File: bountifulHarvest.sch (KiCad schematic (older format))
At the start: 0 parts

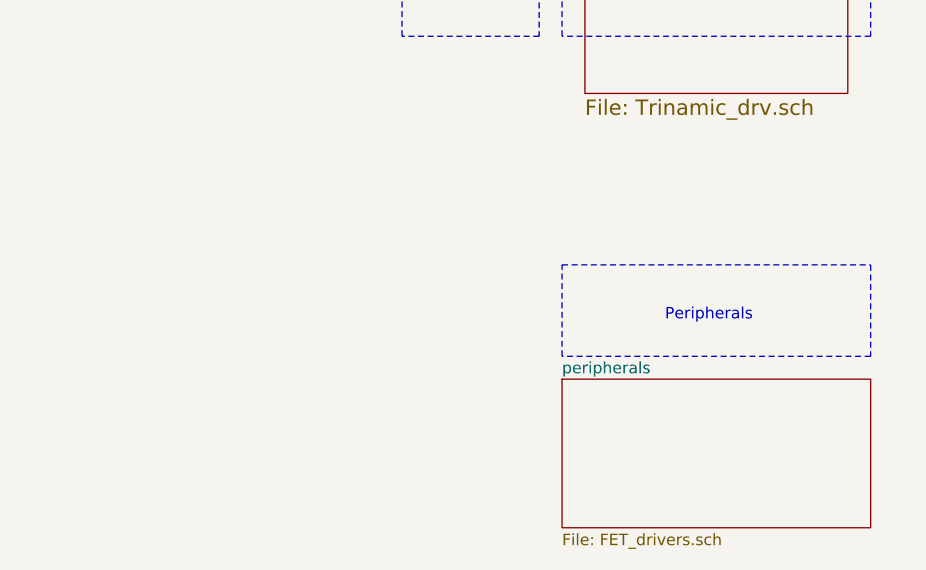
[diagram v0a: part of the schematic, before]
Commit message: Added FET Drivers + PNs. Started Trinamic drivers
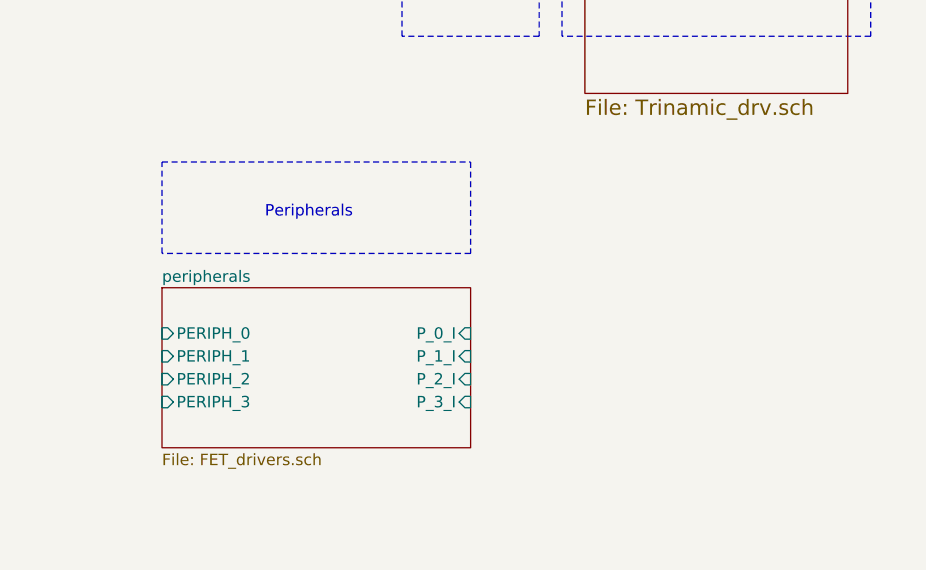
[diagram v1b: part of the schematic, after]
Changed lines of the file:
@@
 $EndSheet
 Wire Notes Line
-	9700 4900 11050 4900
+	7950 4450 9300 4450
 Wire Notes Line
-	11050 4900 11050 5300
+	9300 4450 9300 4850
 Wire Notes Line
-	11050 5300 9700 5300
+	9300 4850 7950 4850
 Wire Notes Line
-	9700 5300 9700 4900
-Text Notes 10150 5150 0    50   ~ 0
+	7950 4850 7950 4450
+Text Notes 8400 4700 0    50   ~ 0
 Peripherals\n
 Wire Notes Line
@@
 $EndSheet
 $Sheet
-S 9700 5400 1350 650
+S 7950 5000 1350 700
 U 5F08C095
 F0 "peripherals" 50
 F1 "FET_drivers.sch" 50
+F2 "PERIPH_0" I L 7950 5200 50
+F3 "PERIPH_1" I L 7950 5300 50
+F4 "PERIPH_2" I L 7950 5400 50
+F5 "PERIPH_3" I L 7950 5500 50
+F6 "P_0_I" I R 9300 5200 50
+F7 "P_3_I" I R 9300 5500 50
+F8 "P_1_I" I R 9300 5300 50
+F9 "P_2_I" I R 9300 5400 50
 $EndSheet
 $EndSCHEMATC

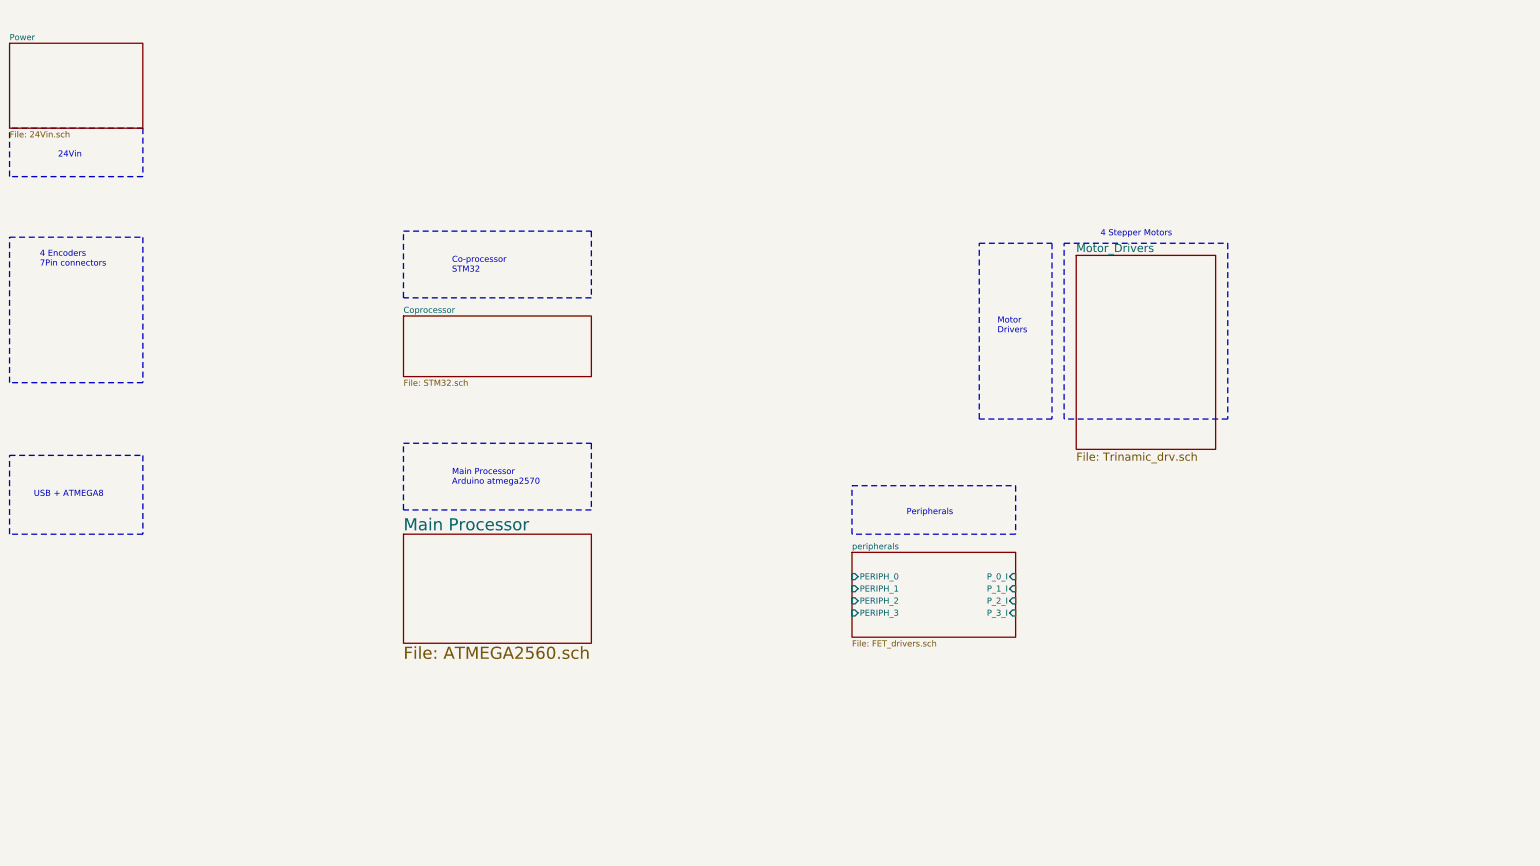
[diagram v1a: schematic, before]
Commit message: Added all stepper circuits. Adding SPI bus to top level sheet. Opened up layout to check connectivity. Errors with footprint libs
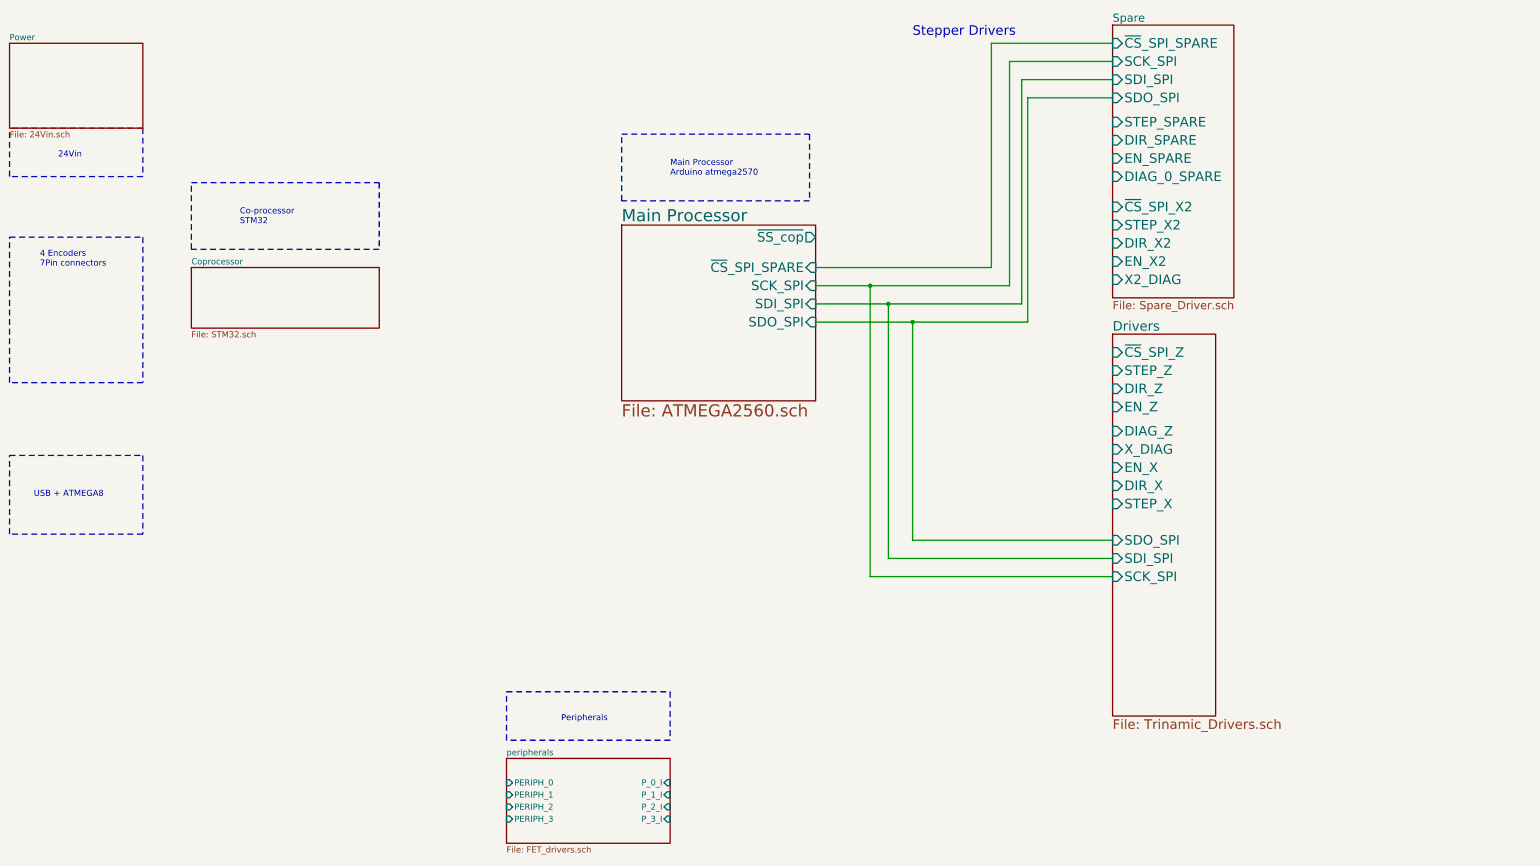
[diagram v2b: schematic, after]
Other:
- note added: "Stepper Drivers"
- note removed: "4 Stepper Motors"
- note removed: "Motor \nDrivers"
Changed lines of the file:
@@
 EESchema Schematic File Version 4
-LIBS:bountifulHarvest-cache
-EELAYER 26 0
+EELAYER 30 0
 EELAYER END
 $Descr A4 11693 8268
 encoding utf-8
-Sheet 1 6
+Sheet 1 7
 Title "BountifulHarvest"
 Date ""
@@
 4 Encoders\n7Pin connectors\n
 Wire Notes Line
-	9700 2450 11050 2450
+	7600 1550 7600 2100
 Wire Notes Line
-	11050 2450 11050 3900
+	7600 2100 6050 2100
 Wire Notes Line
-	11050 3900 9700 3900
+	6050 2100 6050 1550
 Wire Notes Line
-	9700 3900 9700 2450
-Text Notes 10000 2400 0    50   ~ 0
-4 Stepper Motors
-Wire Notes Line
-	5800 4100 5800 4650
-Wire Notes Line
-	5800 4650 4250 4650
-Wire Notes Line
-	4250 4650 4250 4100
-Wire Notes Line
-	4250 4100 5800 4100
-Text Notes 4650 4450 0    50   ~ 0
+	6050 1550 7600 1550
+Text Notes 6450 1900 0    50   ~ 0
 Main Processor\nArduino atmega2570
 Wire Notes Line
-	5800 2350 5800 2900
+	4050 1950 4050 2500
 Wire Notes Line
-	5800 2900 4250 2900
+	4050 2500 2500 2500
 Wire Notes Line
-	4250 2900 4250 2350
+	2500 2500 2500 1950
 Wire Notes Line
-	4250 2350 5800 2350
-Text Notes 4650 2700 0    50   ~ 0
+	2500 1950 4050 1950
+Text Notes 2900 2300 0    50   ~ 0
 Co-processor\nSTM32
-Wire Notes Line
-	9000 2450 9600 2450
-Wire Notes Line
-	9600 2450 9600 3900
-Wire Notes Line
-	9600 3900 9000 3900
-Wire Notes Line
-	9000 3900 9000 2450
-Text Notes 9150 3200 0    50   ~ 0
-Motor \nDrivers
 $Sheet
-S 4250 4850 1550 900
-U 5EE66603
-F0 "Main Processor" 100
-F1 "ATMEGA2560.sch" 100
-$EndSheet
-$Sheet
-S 4250 3050 1550 500
+S 2500 2650 1550 500
 U 5EE7212D
 F0 "Coprocessor" 50
@@
 $EndSheet
 Wire Notes Line
-	7950 4450 9300 4450
-Wire Notes Line
-	9300 4450 9300 4850
-Wire Notes Line
-	9300 4850 7950 4850
-Wire Notes Line
-	7950 4850 7950 4450
-Text Notes 8400 4700 0    50   ~ 0
-Peripherals\n
+	5100 6150 6450 6150
 Wire Notes Line
 	1000 4200 2100 4200
@@
 F1 "24Vin.sch" 50
 $EndSheet
+Text Notes 8450 750  0    79   ~ 0
+Stepper Drivers
 $Sheet
-S 9800 2550 1150 1600
+S 10100 650  1000 2250
 U 5EEE69C6
-F0 "Motor_Drivers" 67
-F1 "Trinamic_drv.sch" 67
+F0 "Spare" 67
+F1 "Spare_Driver.sch" 67
+F2 "~CS~_SPI_SPARE" I L 10100 800 79
+F3 "SCK_SPI" I L 10100 950 79
+F4 "SDI_SPI" I L 10100 1100 79
+F5 "SDO_SPI" I L 10100 1250 79
+F6 "STEP_SPARE" I L 10100 1450 79
+F7 "DIR_SPARE" I L 10100 1600 79
+F8 "EN_SPARE" I L 10100 1750 79
+F9 "~CS~_SPI_X2" I L 10100 2150 79
+F10 "STEP_X2" I L 10100 2300 79
+F11 "DIR_X2" I L 10100 2450 79
+F12 "EN_X2" I L 10100 2600 79
+F13 "X2_DIAG" I L 10100 2750 79
+F14 "DIAG_0_SPARE" I L 10100 1900 79
 $EndSheet
 $Sheet
-S 7950 5000 1350 700
+S 5100 6700 1350 700
 U 5F08C095
 F0 "peripherals" 50
 F1 "FET_drivers.sch" 50
-F2 "PERIPH_0" I L 7950 5200 50
-F3 "PERIPH_1" I L 7950 5300 50
-F4 "PERIPH_2" I L 7950 5400 50
-F5 "PERIPH_3" I L 7950 5500 50
-F6 "P_0_I" I R 9300 5200 50
-F7 "P_3_I" I R 9300 5500 50
-F8 "P_1_I" I R 9300 5300 50
-F9 "P_2_I" I R 9300 5400 50
+F2 "PERIPH_0" I L 5100 6900 50
+F3 "PERIPH_1" I L 5100 7000 50
+F4 "PERIPH_2" I L 5100 7100 50
+F5 "PERIPH_3" I L 5100 7200 50
+F6 "P_0_I" I R 6450 6900 50
+F7 "P_3_I" I R 6450 7200 50
+F8 "P_1_I" I R 6450 7000 50
+F9 "P_2_I" I R 6450 7100 50
 $EndSheet
+Text Notes 5550 6400 0    50   ~ 0
+Peripherals\n
+Wire Notes Line
+	5100 6550 5100 6150
+Wire Notes Line
+	6450 6550 5100 6550
+Wire Notes Line
+	6450 6150 6450 6550
+$Sheet
+S 10100 3200 850  3150
+U 5FF92876
+F0 "Drivers" 79
+F1 "Trinamic_Drivers.sch" 79
+F2 "~CS~_SPI_Z" I L 10100 3350 79
+F3 "STEP_Z" I L 10100 3500 79
+F4 "DIR_Z" I L 10100 3650 79
+F5 "EN_Z" I L 10100 3800 79
+F6 "DIAG_Z" I L 10100 4000 79
+F7 "X_DIAG" I L 10100 4150 79
+F8 "EN_X" I L 10100 4300 79
+F9 "DIR_X" I L 10100 4450 79
+F10 "STEP_X" I L 10100 4600 79
+F11 "SDO_SPI" I L 10100 4900 79
+F12 "SDI_SPI" I L 10100 5050 79
+F13 "SCK_SPI" I L 10100 5200 79
+$EndSheet
+$Sheet
+S 6050 2300 1600 1450
+U 5EE66603
+F0 "Main Processor" 100
+F1 "ATMEGA2560.sch" 100
+F2 "~SS_cop" O R 7650 2400 79
+F3 "~CS~_SPI_SPARE" I R 7650 2650 79
+F4 "SCK_SPI" I R 7650 2800 79
+F5 "SDI_SPI" I R 7650 2950 79
+F6 "SDO_SPI" I R 7650 3100 79
+$EndSheet
+Wire Wire Line
+	7650 2650 9100 2650
+Wire Wire Line
+	9100 2650 9100 800
+Wire Wire Line
+	9100 800  10100 800
+Wire Wire Line
+	10100 950  9250 950
+Wire Wire Line
+	9250 950  9250 2800
+Wire Wire Line
+	9250 2800 8100 2800
+Wire Wire Line
+	10100 1100 9350 1100
+Wire Wire Line
+	9350 1100 9350 2950
+Wire Wire Line
+	9350 2950 8250 2950
+Wire Wire Line
+	7650 3100 8450 3100
+Wire Wire Line
+	9400 3100 9400 1250
+Wire Wire Line
+	9400 1250 10100 1250
+Wire Wire Line
+	10100 5200 8100 5200
+Wire Wire Line
+	8100 5200 8100 2800
+Connection ~ 8100 2800
+Wire Wire Line
+	8100 2800 7650 2800
+Wire Wire Line
+	10100 5050 8250 5050
+Wire Wire Line
+	8250 5050 8250 2950
+Connection ~ 8250 2950
+Wire Wire Line
+	8250 2950 7650 2950
+Wire Wire Line
+	10100 4900 8450 4900
+Wire Wire Line
+	8450 4900 8450 3100
+Connection ~ 8450 3100
+Wire Wire Line
+	8450 3100 9400 3100
 $EndSCHEMATC
